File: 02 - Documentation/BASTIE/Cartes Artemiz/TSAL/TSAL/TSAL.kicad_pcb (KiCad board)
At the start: 2 copper layers, 99.1 x 66 mm, 103 parts, among them J1 2P Droit 2-11-2022, J10 2P Droit 2-11-2022, J11 2P Droit 2-11-2022, J2 2P Droit 2-11-2022, J3 2P Droit 2-11-2022, J4 3P Droit 22-11-2032, J5 2P Droit 2-11-2022, J6 2P Droit 2-11-2022, J7 2P Droit 2-11-2022, J8 2P Droit 2-11-2022, J9 2P Droit 2-11-2022, K1 SSR CPC1394GR, K2 SSR CPC1394GR, K3 SSR CPC1394GR, Q2 NMOS SQ2348ES-T1_GE3, Q4 NMOS SQ2348ES-T1_GE3

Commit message: Corrections mineures
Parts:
- removed ? (x3): , 
- removed J10, J11: 2P Droit 2-11-2022, EPSA_lib:MOLEX_22-11-2022
- removed K1, K2, K3: SSR CPC1394GR, EPSA_lib:CPC1394GR
- removed REF**: MountingHole_3.2mm_M3_DIN965_Pad, MountingHole:MountingHole_3.2mm_M3_DIN965_Pad
- added C20: 10u, EPSA:CAPC2012X130N, B.Cu at (116.5, 63.0)
- added C21: 2.2u, EPSA:CAPC2012X130N, B.Cu at (118.1, 67.6)
- added C22: 2.2u, EPSA:CAPC2012X130N, F.Cu at (135.6, 65.2)
- added C23: 1u, EPSA:CAPC2012X130N, F.Cu at (127.0, 69.7)
- added CP3: Comparator_Quad, Package_SO:TSSOP-14_4.4x5mm_P0.65mm, F.Cu at (123.2, 47.0)
- added CP4: Comparator_Quad, Package_SO:TSSOP-14_4.4x5mm_P0.65mm, F.Cu at (134.0, 47.0)
- added CP5: Comparator_Dual, Package_SO:TSSOP-8_4.4x3mm_P0.65mm, F.Cu at (132.5, 69.2)
- added G14: Gate AND SN74AHCT1G08DBVR, EPSA:SOT95P280X145-5N, F.Cu at (123.8, 67.9)
- added G15: Gate OR SN74AHCT1G32DBVR, EPSA:SOT95P280X145-5N, F.Cu at (116.3, 77.3)
- added G16: Gate NOR SN74AHCT1G02DBVR, EPSA:SOT95P280X145-5N, F.Cu at (120.3, 77.1)
- added H1: MountingHole, MountingHole:MountingHole_3.2mm_M3, F.Cu at (152.8, 30.2)
- added H2: MountingHole, MountingHole:MountingHole_3.2mm_M3, F.Cu at (102.8, 30.2)
- added H3: MountingHole, MountingHole:MountingHole_3.2mm_M3, F.Cu at (102.8, 80.2)
- added H4: MountingHole, MountingHole:MountingHole_3.2mm_M3, F.Cu at (152.8, 80.2)
- added Q1: NMOS SQ2348ES-T1_GE3, EPSA:SOT95P237X112-3N, F.Cu at (145.6, 72.4)
- added Q3: PMOS SI2343CDS-T1-GE3, Package_TO_SOT_SMD:SOT-23-3, F.Cu at (145.8, 76.3)
- added R31: 500, EPSA:RESC3216X70N, B.Cu at (117.5, 51.2)
- added R32: 500, EPSA:RESC3216X70N, B.Cu at (124.8, 41.3)
- added R33: 5k, EPSA:RESC3216X70N, B.Cu at (135.5, 71.2)
- added R34: 500, EPSA:RESC3216X70N, B.Cu at (134.0, 43.2)
- added R35: 500k, EPSA:RESC3216X70N, B.Cu at (126.2, 72.5)
- added R36: 5k, EPSA:RESC3216X70N, B.Cu at (129.9, 71.2)
- added R37: 1k, Resistor_SMD:R_1206_3216Metric, F.Cu at (150.7, 74.8)
- added R38: 10k, Resistor_SMD:R_1206_3216Metric, F.Cu at (137.3, 77.9)
- added R40: 100k, Resistor_SMD:R_1206_3216Metric, F.Cu at (145.9, 79.6)
- added Ref**: Val**, EPSA:Mandolule Silk, F.Cu at (132.0, 57.1)
- added U1: Opamp_Quad, Package_SO:TSSOP-14_4.4x5mm_P0.65mm, F.Cu at (128.9, 39.7)
- added U2: Opamp, Package_TO_SOT_SMD:SOT-353_SC-70-5_Handsoldering, F.Cu at (109.3, 66.7)
- C1, C10, C11, C12, C14, C17, C18, C2, C3, C4, C5, C6, C7, C8, C9: value Condensateur 0805Y1000104JXT -> 10u; footprint EPSA_lib:CAPC2012X130N -> EPSA:CAPC2012X130N; moved to B.Cu
- C13: value Condensateur 0805Y1000104JXT -> C; footprint EPSA_lib:CAPC2012X130N -> Capacitor_THT:CP_Radial_D5.0mm_P2.00mm
- C15: value Condensateur 0805Y1000104JXT -> 1u; footprint EPSA_lib:CAPC2012X130N -> EPSA:CAPC2012X130N; moved to B.Cu
- C16: value C -> 10u; footprint Capacitor_THT:CP_Radial_D5.0mm_P2.00mm -> EPSA:CAPC2012X130N; moved to B.Cu
- C19: value Condensateur 0805Y1000104JXT -> 0.01u; footprint EPSA_lib:CAPC2012X130N -> EPSA:CAPC2012X130N; moved to B.Cu
- CP1: value Comparateur Double LM393LVDR -> Comparator; footprint EPSA_lib:SOIC127P600X175-8N -> Package_TO_SOT_SMD:SOT-353_SC-70-5
- CP2: value Comparateur TS391ILT -> Comparator_Dual; footprint EPSA_lib:SOT95P280X145-5N -> Package_SO:TSSOP-8_4.4x3mm_P0.65mm
- D1, D10, D11, D2, D3, D4, D5, D6, D7, D8, D9: footprint LED_THT:LED_D5.0mm -> LED_SMD:LED_0805_2012Metric
- DL1: footprint EPSA_lib:SOIC127P600X175-14N -> EPSA:SOIC127P600X175-14N
- G1, G2, G3, G4, G5, G6: footprint EPSA_lib:SOT95P280X145-5N -> EPSA:SOT95P280X145-5N
- G10, G11, G8: value Gate OR SN74AHCT1G32DBVR -> Gate AND SN74AHCT1G08DBVR; footprint EPSA_lib:SOT95P280X145-5N -> EPSA:SOT95P280X145-5N
- G12: value Gate NOR SN74AHCT1G02DBVR -> Gate OR SN74AHCT1G32DBVR; footprint EPSA_lib:SOT95P280X145-5N -> EPSA:SOT95P280X145-5N
- G13: value Gate OR SN74AHCT1G32DBVR -> Gate NOR SN74AHCT1G02DBVR; footprint EPSA_lib:SOT95P280X145-5N -> EPSA:SOT95P280X145-5N
- G7: value Gate AND SN74AHCT1G08DBVR -> Gate OR SN74AHCT1G32DBVR; footprint EPSA_lib:SOT95P280X145-5N -> EPSA:SOT95P280X145-5N
- G9: value Gate NAND SN74AHCT1G00DBVR -> Gate OR SN74AHCT1G32DBVR; footprint EPSA_lib:SOT95P280X145-5N -> EPSA:SOT95P280X145-5N
- J1, J2, J3, J5, J6, J9: footprint EPSA_lib:MOLEX_22-11-2022 -> EPSA:MOLEX_22-11-2022
- J4: footprint EPSA_lib:MOLEX_22-11-2032 -> EPSA:MOLEX_22-11-2032
- J7: value 2P Droit 2-11-2022 -> 4P Droit 22-11-2042; footprint EPSA_lib:MOLEX_22-11-2022 -> EPSA:MOLEX_22-11-2042
- J8: value 2P Droit 2-11-2022 -> 3P Droit 22-11-2032; footprint EPSA_lib:MOLEX_22-11-2022 -> EPSA:MOLEX_22-11-2032
- PS1: footprint EPSA_lib:TSR-2 -> EPSA:TSR-2
- Q2: footprint EPSA_lib:SOT95P237X112-3N -> EPSA:SOT95P237X112-3N
- Q4: value NMOS SQ2348ES-T1_GE3 -> PMOS SI2343CDS-T1-GE3; footprint EPSA_lib:SOT95P237X112-3N -> Package_TO_SOT_SMD:SOT-23-3
- R1, R10, R29, R3, R5, R8, R9: value Résistance RK73H2BLTDD2152F -> 500; footprint EPSA_lib:RESC3216X70N -> EPSA:RESC3216X70N; moved to B.Cu
- R11, R12, R13, R14, R16: value Résistance RK73H2BLTDD2152F -> 500k; footprint EPSA_lib:RESC3216X70N -> EPSA:RESC3216X70N; moved to B.Cu
- R15: value Résistance RK73H2BLTDD2152F -> 2k; footprint EPSA_lib:RESC3216X70N -> EPSA:RESC3216X70N; moved to B.Cu
- R17: value Résistance RK73H2BLTDD2152F -> 200k; footprint EPSA_lib:RESC3216X70N -> EPSA:RESC3216X70N; moved to B.Cu
- R18, R2, R20, R28, R4, R6, R7: value Résistance RK73H2BLTDD2152F -> 10k; footprint EPSA_lib:RESC3216X70N -> EPSA:RESC3216X70N
- R19: value Résistance RK73H2BLTDD2152F -> 390k; footprint EPSA_lib:RESC3216X70N -> EPSA:RESC3216X70N; moved to B.Cu
- R21, R24: value Résistance RK73H2BLTDD2152F -> 12k; footprint EPSA_lib:RESC3216X70N -> EPSA:RESC3216X70N
- R22, R23: value Résistance RK73H2BLTDD2152F -> 82k; footprint EPSA_lib:RESC3216X70N -> EPSA:RESC3216X70N
- R25: value Résistance RK73H2BLTDD2152F -> 500; footprint EPSA_lib:RESC3216X70N -> EPSA:RESC3216X70N
- R26: value Résistance RK73H2BLTDD2152F -> 100k; footprint EPSA_lib:RESC3216X70N -> EPSA:RESC3216X70N
- R27: value Résistance RK73H2BLTDD2152F -> 50k; footprint EPSA_lib:RESC3216X70N -> EPSA:RESC3216X70N
- R30: value Résistance RK73H2BLTDD2152F -> 500k; footprint EPSA_lib:RESC3216X70N -> EPSA:RESC3216X70N
- RV1: footprint EPSA_lib:3296Y1223LF -> EPSA:3296Y1223LF
- TI1: footprint Package_DIP:DIP-8_W7.62mm_Socket -> EPSA:SOIC127P600X175-8N
- TP1, TP2, TP3, TP4: value TestPoint -> type="R" model="TestPoint" lib=""
- moved R28 89.0 mm to (141.1, 49.2)
- moved C19 83.3 mm to (146.0, 37.6)
- moved R6 78.7 mm to (145.4, 69.2), turned to 0 degrees
- moved R18 77.2 mm to (145.4, 38.7), turned to 0 degrees
- moved J5 77.0 mm to (151.8, 68.9), turned to -90 degrees
- moved G8 70.7 mm to (141.0, 70.5), turned to 90 degrees
- moved R26 68.1 mm to (131.8, 63.5), turned to 180 degrees
- moved J7 67.4 mm to (128.9, 32.9)
- moved C15 64.6 mm to (140.3, 32.9), turned to -90 degrees
- moved R3 63.9 mm to (106.7, 38.6), turned to 180 degrees
- moved D1 59.0 mm to (107.4, 38.5), turned to 0 degrees
- moved R29 58.5 mm to (129.5, 50.2), turned to 180 degrees
- moved D11 58.0 mm to (135.3, 40.6), turned to -90 degrees
- moved R27 56.8 mm to (131.8, 66.0), turned to 0 degrees
- moved D10 56.6 mm to (121.6, 41.9), turned to 0 degrees
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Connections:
- C1 pad 1: 0 -> GND
- C1 pad 2: Net-(C1-Pad2) -> +5V
- C10 pad 1: 0 -> GND
- C11 pad 1: 0 -> GND
- C12 pad 1: 0 -> GND
- C13 pad 1: 0 -> GND
- C13 pad 2: +5V -> +12V
- C14 pad 1: 0 -> GND
- C15 pad 1: 0 -> GND
- C15 pad 2: +5V -> Net-(TI1-THRESHOLD)
- C16 pad 1: 0 -> GND
- C16 pad 2: +12V -> +5V
- C17 pad 1: 0 -> GND
- C18 pad 1: 0 -> GND
- C19 pad 1: 0 -> GND
- C19 pad 2: +5V -> Net-(TI1-CONTROL_VOLTAGE)
- C2 pad 1: +5V -> GND
- C2 pad 2: 0 -> +5V
- C3 pad 1: 0 -> GND
- C3 pad 2: Net-(C3-Pad2) -> +5V
- C4 pad 1: Net-(C4-Pad1) -> GND
- C4 pad 2: 0 -> +5V
- C5 pad 1: 0 -> GND
- C5 pad 2: Net-(C5-Pad2) -> +5V
- C6 pad 1: 0 -> GND
- C6 pad 2: Net-(C6-Pad2) -> +5V
- C7 pad 1: 0 -> GND
- C8 pad 1: 0 -> GND
- C9 pad 1: 0 -> GND
- CP1 pad 1: CLR -> Net-(CP1-+)
- CP1 pad 2: mid Pot -> GND
- CP1 pad 3: Net-(C1-Pad2) -> Net-(CP1--)
- CP1 pad 4: 0 -> /Int_del
- CP1 pad 5: Net-(C3-Pad2) -> +5V
- CP2 pad 1: SCS del -> /SCS compliance
- CP2 pad 2: 0 -> /DC-Link_In
- CP2 pad 3: Net-(CP2-Pad3) -> /4.25V
- CP2 pad 4: Net-(C4-Pad1) -> GND
- CP2 pad 5: +5V -> /DC-Link_In
- D1 pad 1: AIR 1 -> /AIR_1
- D1 pad 2: Net-(D1-Pad2) -> Net-(D1-A)
- D10 pad 1: 0 -> GND
- D10 pad 2: Net-(D10-Pad2) -> Net-(D10-A)
- D11 pad 1: 0 -> GND
- D11 pad 2: Net-(D11-Pad2) -> Net-(D11-A)
- D2 pad 1: 0 -> Net-(D2-K)
- D2 pad 2: Net-(D2-Pad2) -> +5V
- D3 pad 1: AIR 2 -> /AIR_2
- D3 pad 2: Net-(D3-Pad2) -> Net-(D3-A)
- D4 pad 1: PreCharge -> /PreCharge
- D4 pad 2: Net-(D4-Pad2) -> Net-(D4-A)
- D5 pad 1: 0 -> GND
- D5 pad 2: Net-(D5-Pad2) -> Net-(D5-A)
- D6 pad 1: 0 -> Net-(D6-K)
- D6 pad 2: Net-(D6-Pad2) -> +5V
- D7 pad 1: 0 -> GND
- D7 pad 2: Net-(D7-Pad2) -> Net-(D7-A)
- D8 pad 1: 0 -> GND
- D8 pad 2: Net-(D8-Pad2) -> Net-(D8-A)
- D9 pad 1: 0 -> GND
- D9 pad 2: Net-(D9-Pad2) -> Net-(D9-A)
- DL1 pad 1: CLR -> /CLR
- DL1 pad 10: 0 -> GND
- DL1 pad 11: 0 -> GND
- DL1 pad 12: 0 -> GND
- DL1 pad 13: 0 -> GND
- DL1 pad 2: 0 -> GND
- DL1 pad 3: SCS del -> /Int_del
- DL1 pad 4: PRE -> /PRE
- DL1 pad 5: SCS -> /INT
- DL1 pad 7: 0 -> GND
- G1 pad 1: AIR 1 -> /AIR_1
- G1 pad 2: AIR 2 -> /AIR_2
- G1 pad 3: 0 -> GND
- G10 pad 1: Int AIR 2 -> Net-(G1-Pad4)
- G10 pad 2: Int PreCharge -> Net-(G10-Pad2)
- G10 pad 3: 0 -> GND
- G10 pad 4: Net-(G10-Pad4) -> /Lightning_cond
- G11 pad 2: Net-(G11-Pad2) -> /VoltageAIR
- G11 pad 3: 0 -> GND
- G12 pad 2: VoltageAIR -> Net-(G12-Pad2)
- G12 pad 3: 0 -> GND
- G13 pad 3: 0 -> GND
- G13 pad 4: SCS log -> Net-(G13-Pad4)
- G2 pad 1: PreCharge -> /PreCharge
- G2 pad 2: VoltageAIR -> /VoltageAIR
- G2 pad 3: 0 -> GND
- G2 pad 4: Net-(G2-Pad4) -> Net-(G10-Pad2)
- G3 pad 1: AIR 1 -> /AIR_1
- G3 pad 2: Int AIR 1 -> /Int_AIR_1
- G3 pad 3: 0 -> GND
- G4 pad 1: AIR 2 -> /AIR_2
- G4 pad 2: Int AIR 2 -> /Int_AIR_2
- G4 pad 3: 0 -> GND
- G5 pad 1: PreCharge -> /PreCharge
- G5 pad 2: Int PreCharge -> /Int_PreCharge
- G5 pad 3: 0 -> GND
- G5 pad 4: Net-(G11-Pad2) -> Net-(G12-Pad2)
- G6 pad 1: Lightning cond -> Net-(G6-Pad1)
- G6 pad 2: SCS -> /Int_AIR_1
- G6 pad 3: 0 -> GND
- G6 pad 4: Net-(G6-Pad4) -> Net-(G11-Pad1)
- G7 pad 1: Net-(G2-Pad4) -> /Int_AIR_2
- G7 pad 2: Net-(G1-Pad4) -> /Int_PreCharge
- G7 pad 3: 0 -> GND
- G7 pad 4: Lightning cond -> Net-(G6-Pad1)
- G8 pad 1: Net-(G3-Pad4) -> /Lightning_cond
- G8 pad 2: Net-(G4-Pad4) -> /INT
- G8 pad 3: 0 -> GND
- G8 pad 4: Net-(G11-Pad1) -> Net-(G8-Pad4)
- G9 pad 1: Net-(G10-Pad4) -> Net-(G3-Pad4)
- G9 pad 2: Int AIR 1 -> Net-(G4-Pad4)
- G9 pad 3: 0 -> GND
- J1 pad 1: 0 -> GND
- J1 pad 2: AIR 1 -> /AIR_1
- J2 pad 1: 0 -> GND
- J2 pad 2: AIR 2 -> /AIR_2
- J3 pad 1: 0 -> GND
- J3 pad 2: PreCharge -> /PreCharge
- J4 pad 1: 0 -> GND
- J4 pad 3: VoltageAIR -> /Raw_VoltageAIR
- J5 pad 1: Net-(J5-Pad1) -> +12V
- J6 pad 1: +12V -> GND
- J6 pad 2: Net-(J6-Pad2) -> +12V
- J7 pad 1: Net-(J7-Pad1) -> GND
- J7 pad 2: Net-(J7-Pad2) -> /Raw_Int_AIR_1
- J8 pad 1: Net-(J8-Pad1) -> GND
- J8 pad 2: Net-(J8-Pad2) -> +5V
- J9 pad 1: 0 -> +12V
- J9 pad 2: DC-Link In -> Net-(J9-Pad2)
- PS1 pad 2: 0 -> GND
- Q2 pad 1: Net-(G6-Pad4) -> Net-(Q2-Pad1)
- Q2 pad 2: 0 -> GND
- Q2 pad 3: Net-(J6-Pad2) -> Net-(J9-Pad2)
- Q4 pad 1: Clign -> Net-(Q3-Pad1)
- Q4 pad 2: 0 -> /dis2
- R1 pad 1: mid Pot -> /INT
- R1 pad 2: +5V -> Net-(D2-K)
- R10 pad 1: PRE -> Net-(G15-Pad4)
- R10 pad 2: +5V -> Net-(D6-K)
- R11 pad 1: Net-(D5-Pad2) -> GND
- R11 pad 2: VoltageAIR -> /Raw_Int_AIR_1
- R12 pad 1: 0 -> GND
- R12 pad 2: Net-(C3-Pad2) -> /Raw_Int_AIR_2
- R13 pad 1: Lightning cond -> GND
- R13 pad 2: Net-(D6-Pad2) -> /Raw_DC-Link_In
- R14 pad 1: Net-(C3-Pad2) -> GND
- R14 pad 2: +5V -> /Raw_Int_PreCharge
- R15 pad 1: SCS log -> Net-(TI1-DISCHARGE)
- R15 pad 2: Net-(D7-Pad2) -> /DC-Link_In
- R16 pad 1: Net-(D8-Pad2) -> GND
- R16 pad 2: DC-Link In -> /Raw_VoltageAIR
- R17 pad 1: Net-(J5-Pad2) -> Net-(TI1-THRESHOLD)
- R17 pad 2: Net-(K1-Pad1) -> Net-(TI1-DISCHARGE)
- R18 pad 1: Net-(J7-Pad2) -> /Clign
- R18 pad 2: Net-(K2-Pad1) -> Net-(Q2-Pad1)
- R19 pad 1: +5V -> Net-(G15-Pad4)
- R19 pad 2: SCS del -> Net-(CP1-+)
- R2 pad 1: 0 -> /AIR_1
- R2 pad 2: mid Pot -> +5V
- R20 pad 1: SCS log -> /Int_del
- R20 pad 2: Net-(C4-Pad1) -> +5V
- R21 pad 1: Net-(C4-Pad1) -> /4.25V
- R21 pad 2: 0 -> +5V
- R22 pad 1: Net-(J8-Pad2) -> GND
- R22 pad 2: Net-(K3-Pad1) -> /4.25V
- R23 pad 1: Net-(R23-Pad1) -> /0.75V
- R23 pad 2: DC-Link In -> +5V
- R24 pad 1: Net-(C5-Pad2) -> GND
- R24 pad 2: Net-(R23-Pad1) -> /0.75V
- R25 pad 1: Int AIR 1 -> Net-(D7-A)
- R25 pad 2: Net-(D9-Pad2) -> /VoltageAIR
- R26 pad 1: Int AIR 2 -> /mid_Pot
- R26 pad 2: Net-(D10-Pad2) -> +5V
- R27 pad 1: Int PreCharge -> GND
- R27 pad 2: Net-(D11-Pad2) -> /mid_Pot
- R28 pad 1: Net-(D1-Pad2) -> +5V
- R28 pad 2: +5V -> /SCS compliance
- R29 pad 1: Net-(D3-Pad2) -> Net-(D8-A)
- R29 pad 2: +5V -> /DC-Link_In
- R3 pad 1: AIR 1 -> Net-(D1-A)
- R30 pad 1: Net-(D4-Pad2) -> /dis1
- R4 pad 1: Net-(C1-Pad2) -> /AIR_2
- R5 pad 1: 0 -> Net-(D3-A)
- R5 pad 2: Net-(C1-Pad2) -> +5V
- R6 pad 1: AIR 2 -> Net-(G8-Pad4)
- R6 pad 2: +5V -> Net-(Q1-Pad1)
- R7 pad 1: CLR -> /PreCharge
- R8 pad 1: SCS -> Net-(D4-A)
- R8 pad 2: Net-(D2-Pad2) -> +5V
- R9 pad 1: PreCharge -> /Lightning_cond
- R9 pad 2: +5V -> Net-(D5-A)
- RV1 pad 2: Net-(CP2-Pad3) -> Net-(CP1--)
- RV1 pad 3: 0 -> GND
- TI1 pad 1: 0 -> GND
- TI1 pad 2: Net-(C5-Pad2) -> Net-(TI1-THRESHOLD)
- TI1 pad 3: Clign -> /Clign
- TI1 pad 4: DC-Link In -> /DC-Link_In
- TI1 pad 5: Net-(C6-Pad2) -> Net-(TI1-CONTROL_VOLTAGE)
- TI1 pad 6: Net-(C5-Pad2) -> Net-(TI1-THRESHOLD)
- TI1 pad 7: Net-(R23-Pad1) -> Net-(TI1-DISCHARGE)
- TP1 pad 1: CLR -> /Int_log
- TP2 pad 1: PRE -> /Int_del
- TP3 pad 1: SCS log -> /PRE
- TP4 pad 1: SCS del -> /CLR
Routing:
- net +5V: track 537.1 -> 403.8 mm, vias 2 -> 33
- net GND: track 0.00 -> 103.8 mm, vias 0 -> 28
- net AIR 1: track 72.2 -> 0.00 mm, vias 1 -> 0
- net /VoltageAIR: track 0.00 -> 72.1 mm, vias 0 -> 2
- net VoltageAIR: track 67.7 -> 0.00 mm
- net Int AIR 2: track 67.3 -> 0.00 mm, vias 3 -> 0
- net /Int_PreCharge: track 0.00 -> 66.3 mm, vias 0 -> 2
- net /SCS compliance: track 0.00 -> 59.4 mm, vias 0 -> 2
- net Int PreCharge: track 58.7 -> 0.00 mm, vias 3 -> 0
- net AIR 2: track 55.5 -> 0.00 mm, vias 1 -> 0
- net PreCharge: track 54.9 -> 0.00 mm
- net /Int_AIR_2: track 0.00 -> 54.3 mm, vias 0 -> 4
- net /0.75V: track 0.00 -> 52.9 mm, vias 0 -> 7
- net Lightning cond: track 46.8 -> 0.00 mm, vias 2 -> 0
- net Int AIR 1: track 45.9 -> 0.00 mm
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- added copper zone on B.Cu, net GND
- added copper zone on F.Cu, net GND
- removed copper zone on B.Cu, net 0
- removed copper zone on F.Cu, net 0
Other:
- board size 99.1 x 66 mm -> 58 x 58 mm
- board text added: "1"
- board text added: "12V"
- board text added: "2"
- board text added: "50mm x 50mm"
- board text added: "5V"
- board text added: "AIR 1"
- board text added: "AIR 2"
- board text added: "Alim"
- board text added: "DCi"
- board text added: "EPSA"
- board text added: "FailDel"
- board text added: "G"
- board text added: "Green TSAL"
- board text added: "I1"
- board text added: "I2"
- board text added: "IP"
- board text added: "Input"
- board text added: "IntF"
- board text added: "Intentionnal"
- board text added: "LC"
- board text added: "Latch"
- board text added: "Mounting holes"
- board text added: "P"
- board text added: "Red TSAL"
- board text added: "S"
- board text added: "TSAL V2.0"
- board text added: "VAIR"
- board text removed: "+"
- board text removed: "+12V"
- board text removed: "+5V"
- board text removed: "-"
- board text removed: "Air 1-"
- board text removed: "Air 2+"
- board text removed: "Air Voltage"
- board text removed: "Air1"
- board text removed: "Air2"
- board text removed: "Alimentation"
- board text removed: "DC-Link In"
- board text removed: "Green"
- board text removed: "Int Air 1-"
- board text removed: "Int Air 2+"
- board text removed: "Int Air1"
- board text removed: "Int Air2"
- board text removed: "Int Pre"
- board text removed: "Light cond"
- board text removed: "Pre"
- board text removed: "Red"
- board text removed: "SCS"
- board text removed: "SCS log"
- board text removed: "SCSdel"
- board text removed: "VA"

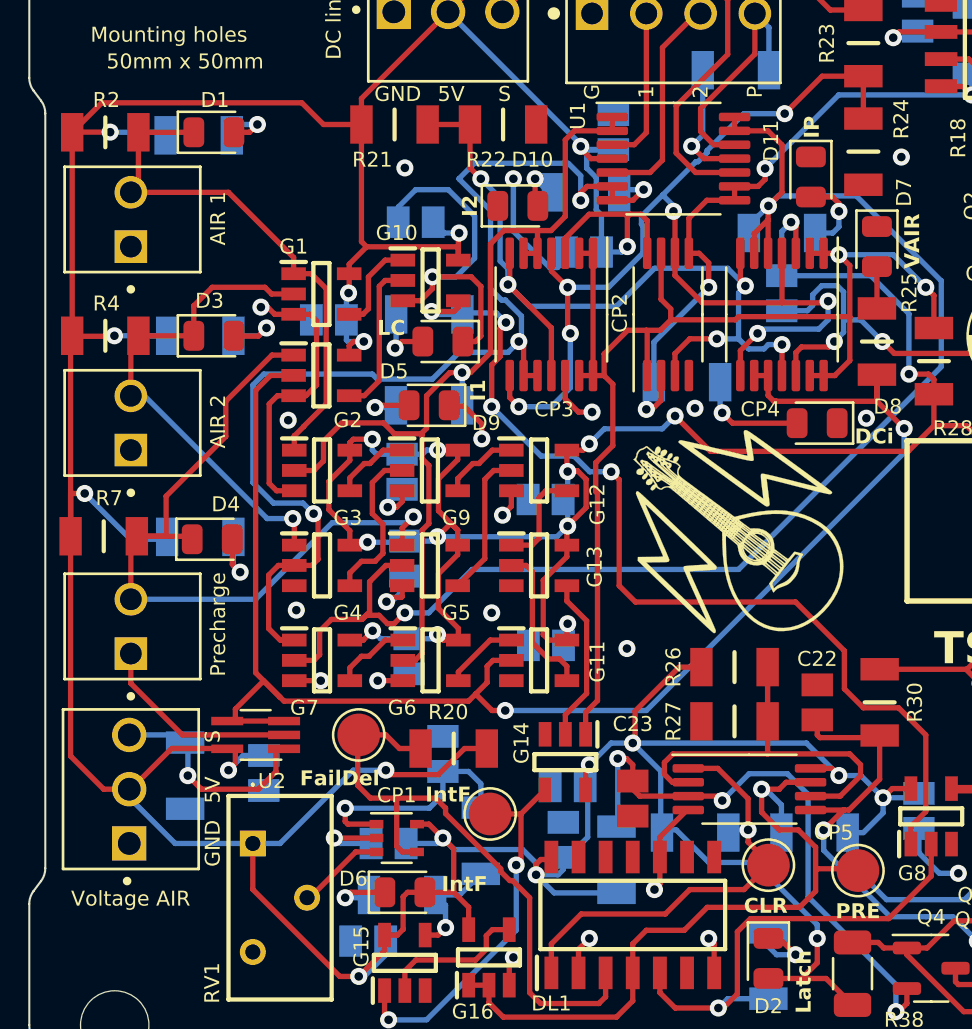
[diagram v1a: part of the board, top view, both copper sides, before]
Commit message: Modifications cartes
Prise en compte des retours ECT + PCBs
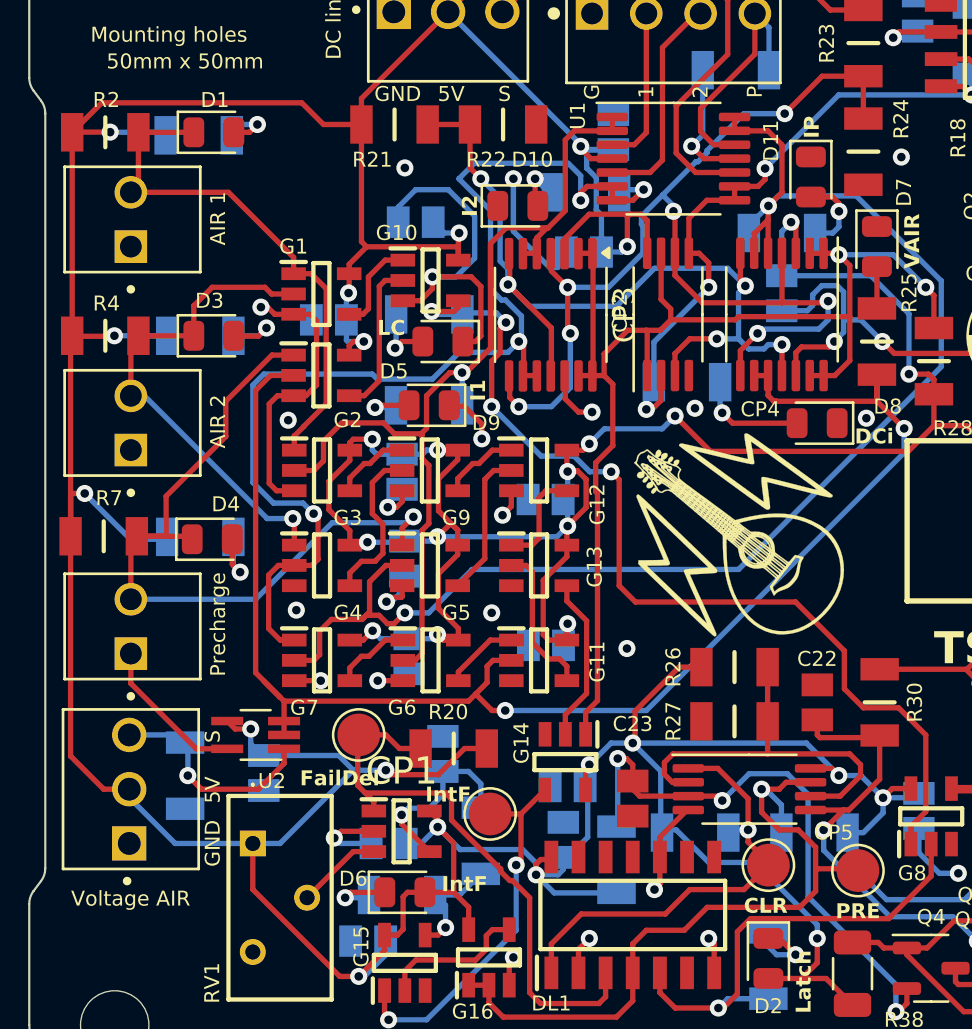
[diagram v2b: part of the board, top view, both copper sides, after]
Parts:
- CP1: value Comparator -> Comparateur TS391ILT; footprint Package_TO_SOT_SMD:SOT-353_SC-70-5 -> EPSA_lib:SOT95P280X145-5N
- moved CP1 0.39 mm to (116.2, 71.2)
- moved Ref** 0.15 mm to (132.0, 57.3)
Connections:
- C21 pad 1: Net-(CP1-+) -> Net-(CP1-IN+)
- CP1 pad 1: Net-(CP1-+) -> /Int_del
- CP1 pad 4: /Int_del -> Net-(CP1-IN+)
- R19 pad 2: Net-(CP1-+) -> Net-(CP1-IN+)
- U2 pad 2: GND -> /VoltageAIR
- U2 pad 4: /VoltageAIR -> +5V
- U2 pad 5: +5V -> GND
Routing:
- net Net-(CP1-+): track 11.2 -> 0.00 mm, vias 1 -> 0
- net Net-(CP1-IN+): track 0.00 -> 8.80 mm, vias 0 -> 1
- net /VoltageAIR: track 72.1 -> 69.3 mm
- net /Int_del: track 28.6 -> 26.8 mm
- net GND: track 103.8 -> 102.0 mm
- net +5V: track 403.8 -> 402.9 mm

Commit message: Vérification PCBs + Fichiers Fabrication
Préparation pour production des PCBs
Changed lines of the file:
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@@
 			(drillshape 0)
 			(scaleselection 1)
-			(outputdirectory "Cirly/")
+			(outputdirectory "../../Cirly/TSAL ECT/")
 		)
 	)
@@
 			(size 1.125 1.75)
 			(layers "F.Cu" "F.Paste" "F.Mask")
-			(roundrect_rratio 0.222222)
+			(roundrect_rratio 0.2222222222)
 			(net 2 "+5V")
 			(pintype "passive")
@@
 			(size 1.125 1.75)
 			(layers "F.Cu" "F.Paste" "F.Mask")
-			(roundrect_rratio 0.222222)
+			(roundrect_rratio 0.2222222222)
 			(net 67 "Net-(Q3-Pad1)")
 			(pintype "passive")
@@
 			(size 1.125 1.75)
 			(layers "F.Cu" "F.Paste" "F.Mask")
-			(roundrect_rratio 0.222222)
+			(roundrect_rratio 0.2222222222)
 			(net 67 "Net-(Q3-Pad1)")
 			(pintype "passive")
@@
 			(size 1.125 1.75)
 			(layers "F.Cu" "F.Paste" "F.Mask")
-			(roundrect_rratio 0.222222)
+			(roundrect_rratio 0.2222222222)
 			(net 13 "GND")
 			(pintype "passive")
@@
 			(size 1.125 1.75)
 			(layers "F.Cu" "F.Paste" "F.Mask")
-			(roundrect_rratio 0.222222)
+			(roundrect_rratio 0.2222222222)
 			(net 13 "GND")
 			(pintype "passive")
@@
 			(size 1.125 1.75)
 			(layers "F.Cu" "F.Paste" "F.Mask")
-			(roundrect_rratio 0.222222)
+			(roundrect_rratio 0.2222222222)
 			(net 68 "Net-(Q3-Pad3)")
 			(pintype "passive")

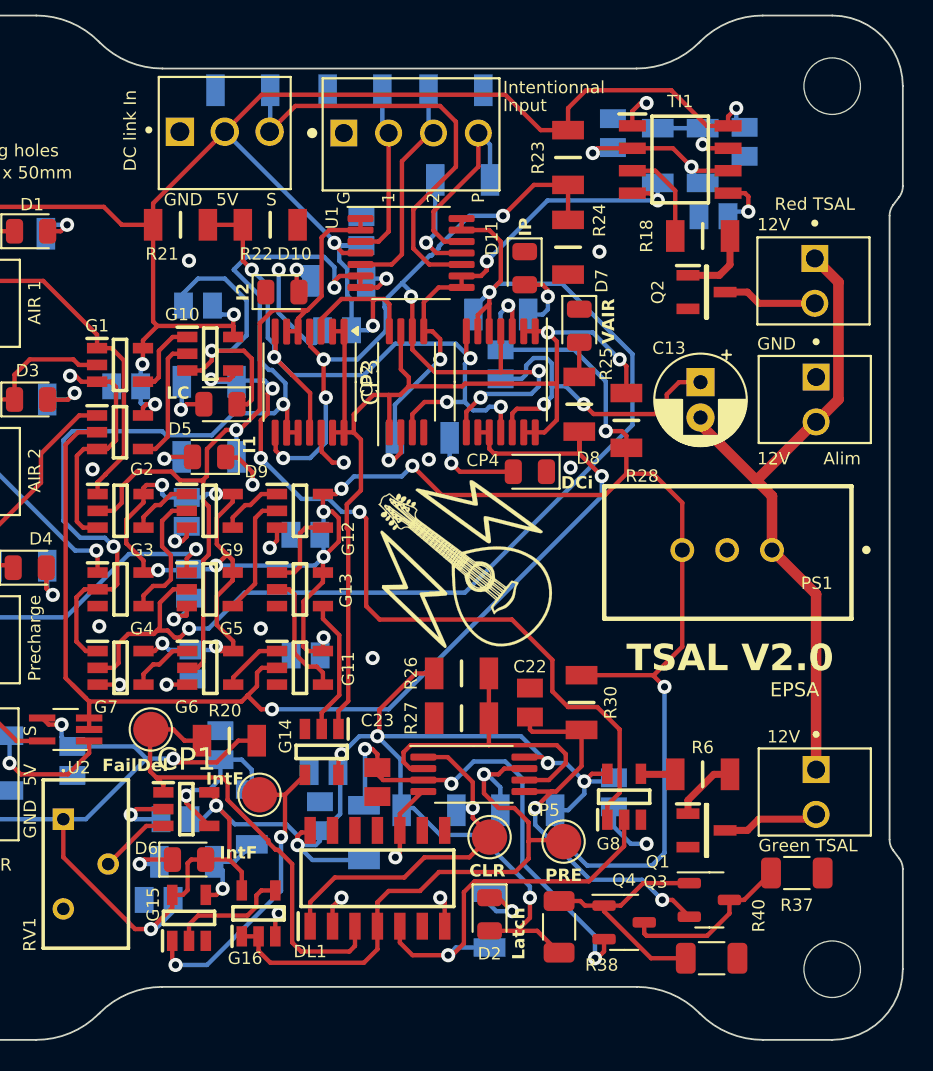
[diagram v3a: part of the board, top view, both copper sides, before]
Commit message: PCBs + fichiers de fabrication
Update SCS LEDs et retours TSAL ESF
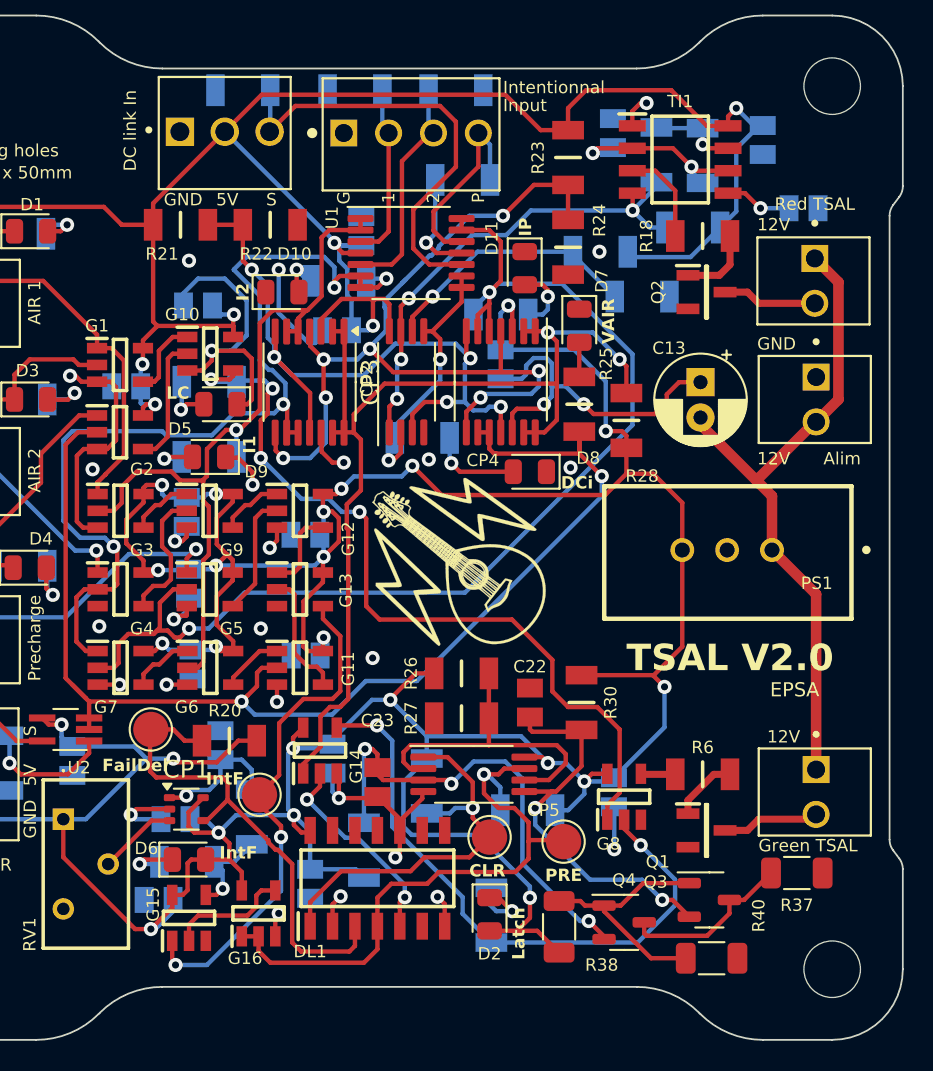
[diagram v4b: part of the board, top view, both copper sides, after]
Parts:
- added R39: 10k, EPSA:RESC3216X70N, B.Cu at (144.9, 38.3)
- added R41: 12k, EPSA:RESC3216X70N, B.Cu at (139.6, 39.6)
- added R42: 12k, EPSA:RESC3216X70N, B.Cu at (142.0, 42.2)
- CP1: value Comparateur TS391ILT -> Comparator; footprint EPSA_lib:SOT95P280X145-5N -> Package_TO_SOT_SMD:SOT-353_SC-70-5
- moved C19 5.12 mm to (151.1, 37.2), turned to 180 degrees
- moved C1 3.87 mm to (123.2, 75.4), turned to 90 degrees
- moved R36 1.38 mm to (129.8, 69.9), turned to 90 degrees
- moved C5 1.03 mm to (148.8, 33.3)
- moved R35 0.99 mm to (126.2, 73.5)
- moved C14 0.92 mm to (124.5, 68.3), turned to 90 degrees
- moved Ref** 0.38 mm to (131.6, 57.2)
- moved R1 0.30 mm to (133.5, 77.2)
- moved G14 0.12 mm to (123.7, 67.9), turned to 90 degrees
- moved R15 0.09 mm to (142.8, 34.1)
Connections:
- C21 pad 1: Net-(CP1-IN+) -> Net-(CP1-+)
- CP1 pad 1: /Int_del -> Net-(CP1-+)
- CP1 pad 4: Net-(CP1-IN+) -> /Int_del
- CP2 pad 1: /SCS compliance -> /DC-Link_In_SCS
- CP2 pad 6: /0.75V -> /2.5V
- CP2 pad 7: /SCS compliance -> /DC-Link_In_SCS
- G13 pad 4: Net-(G13-Pad4) -> /Int_log
- G14 pad 2: Net-(G13-Pad4) -> /INT
- G14 pad 4: /Int_log -> Net-(G14-Pad4)
- G8 pad 2: /INT -> Net-(G14-Pad4)
- R1 pad 1: /INT -> Net-(G14-Pad4)
- R15 pad 2: /DC-Link_In -> /DC-Link_In_SCS
- R19 pad 2: Net-(CP1-IN+) -> Net-(CP1-+)
- TI1 pad 4: /DC-Link_In -> /DC-Link_In_SCS
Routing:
- net Net-(G14-Pad4): track 0.00 -> 34.6 mm, vias 0 -> 2
- net /DC-Link_In_SCS: track 0.00 -> 28.2 mm, vias 0 -> 4
- net /DC-Link_In: track 31.2 -> 14.5 mm, vias 4 -> 2
- net /2.5V: track 0.00 -> 15.0 mm, vias 0 -> 1
- net /Int_log: track 17.7 -> 29.1 mm
- net /INT: track 22.2 -> 11.8 mm, vias 1 -> 2
- net Net-(CP1-IN+): track 8.80 -> 0.00 mm, vias 1 -> 0
- net GND: track 102.0 -> 110.0 mm, vias 28 -> 30
- net Net-(G13-Pad4): track 7.75 -> 0.00 mm
- net Net-(CP1-+): track 0.00 -> 7.54 mm, vias 0 -> 1
- net +5V: track 402.9 -> 408.7 mm
- net /SCS compliance: track 59.4 -> 57.6 mm
- net /CLR: track 20.7 -> 22.4 mm
- net /0.75V: track 52.9 -> 51.6 mm
- net /dis2: track 27.2 -> 26.4 mm
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
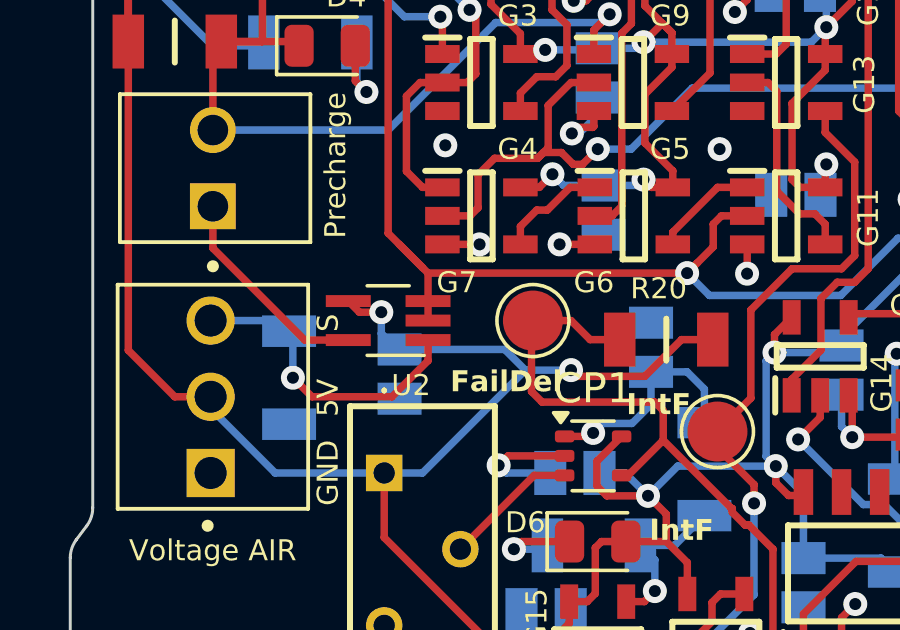
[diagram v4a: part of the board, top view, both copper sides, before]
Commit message: correct opamp tsal
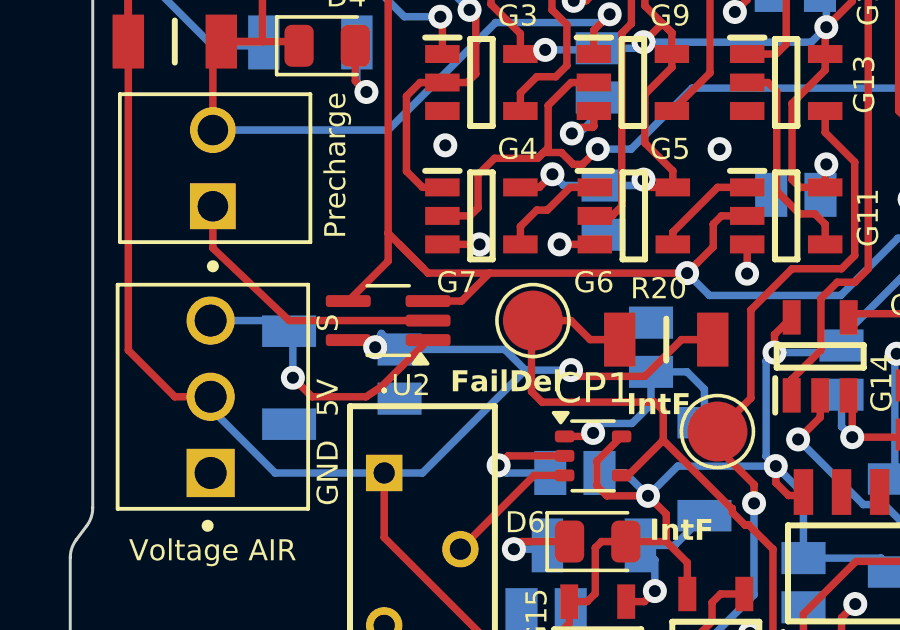
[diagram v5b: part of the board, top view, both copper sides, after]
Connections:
- U2 pad 2: /VoltageAIR -> GND
- U2 pad 4: +5V -> /VoltageAIR
- U2 pad 5: GND -> +5V
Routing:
- net /VoltageAIR: track 69.8 -> 73.4 mm
- net GND: track 110.0 -> 112.4 mm

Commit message: Aop fixes
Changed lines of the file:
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@@
-	)
-	(segment
-		(start 108.6762 67.325)
-		(end 108.9152 67.564)
-		(width 0.25)
-		(layer "F.Cu")
-		(net 1)
 	)
 	(segment
@@
 	)
 	(segment
+		(start 108.256 67.564)
+		(end 108.017 67.325)
+		(width 0.25)
+		(layer "F.Cu")
+		(net 1)
+	)
+	(segment
 		(start 144.26232 53.83832)
 		(end 144.26232 61.98568)
@@
 	)
 	(segment
+		(start 108.9152 67.564)
+		(end 108.256 67.564)
+		(width 0.25)
+		(layer "F.Cu")
+		(net 1)
+	)
+	(segment
 		(start 118.805 53.345)
 		(end 117.8645 53.345)
@@
 		(width 0.25)
 		(layer "F.Cu")
-		(net 1)
-	)
-	(segment
-		(start 108.017 67.325)
-		(end 108.6762 67.325)
-		(width 0.25)
-		(layer "F.Cu")
